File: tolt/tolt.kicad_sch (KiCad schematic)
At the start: 0 parts

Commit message: new file:   tolt/powerstage.kicad_sch 	modified:   tolt/stm32.kicad_sch 	modified:   tolt/tolt.kicad_pro 	modified:   tolt/tolt.kicad_sch
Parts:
- added J2: USB_C_Receptacle_USB2.0, Connector_USB:USB_C_Receptacle_G-Switch_GT-USB-7051x, symbol Connector:USB_C_Receptacle_USB2.0
- added R4, R5: 5k1, Resistor_SMD:R_0603_1608Metric, symbol Device:R
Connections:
- new net: J2.B5 (CC2), R5.2
- new net: J2.A5 (CC1), R4.2
- new net: J2.A4 (VBUS), J2.A9 (VBUS), J2.B4 (VBUS), J2.B9 (VBUS)
- new net: J2.A6 (D+), J2.B6 (D+)
- new net: J2.A7 (D-), J2.B7 (D-)
- new net GND: J2.A1 (GND), J2.A12 (GND), J2.B1 (GND), J2.B12 (GND), J2.S1 (SHIELD), R4.1, R5.1
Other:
- sheet mcu renamed logic
- added sheet powerstage (powerstage.kicad_sch)

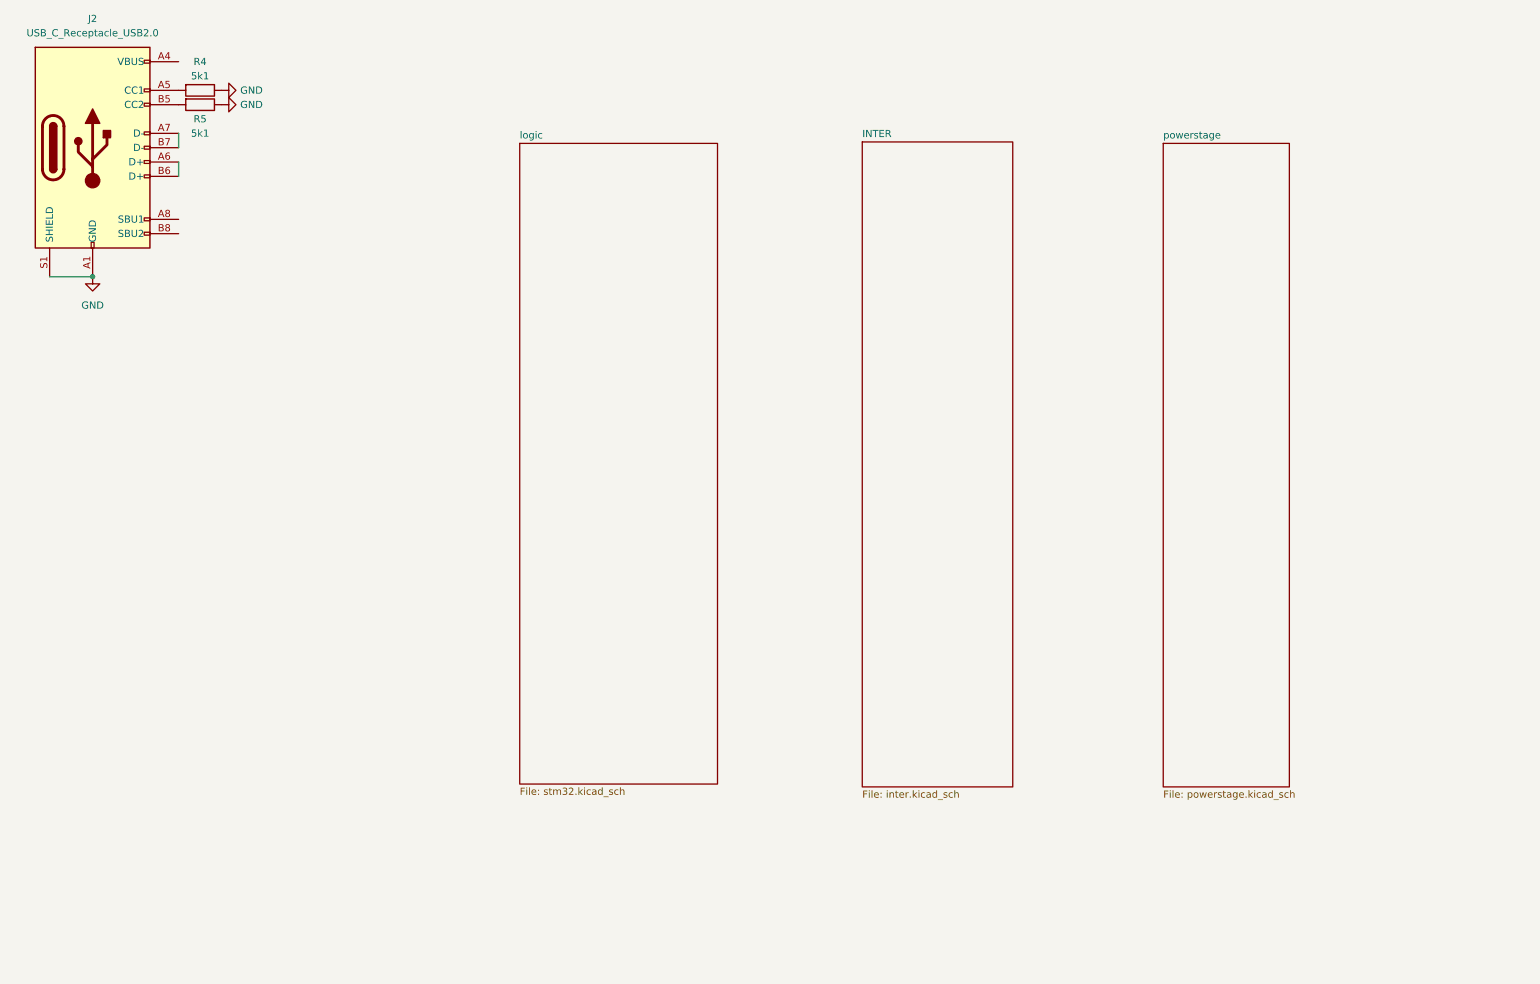
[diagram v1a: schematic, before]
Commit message: modified:   tolt/inter.kicad_sch 	modified:   tolt/stm32.kicad_sch 	modified:   tolt/tolt.kicad_sch
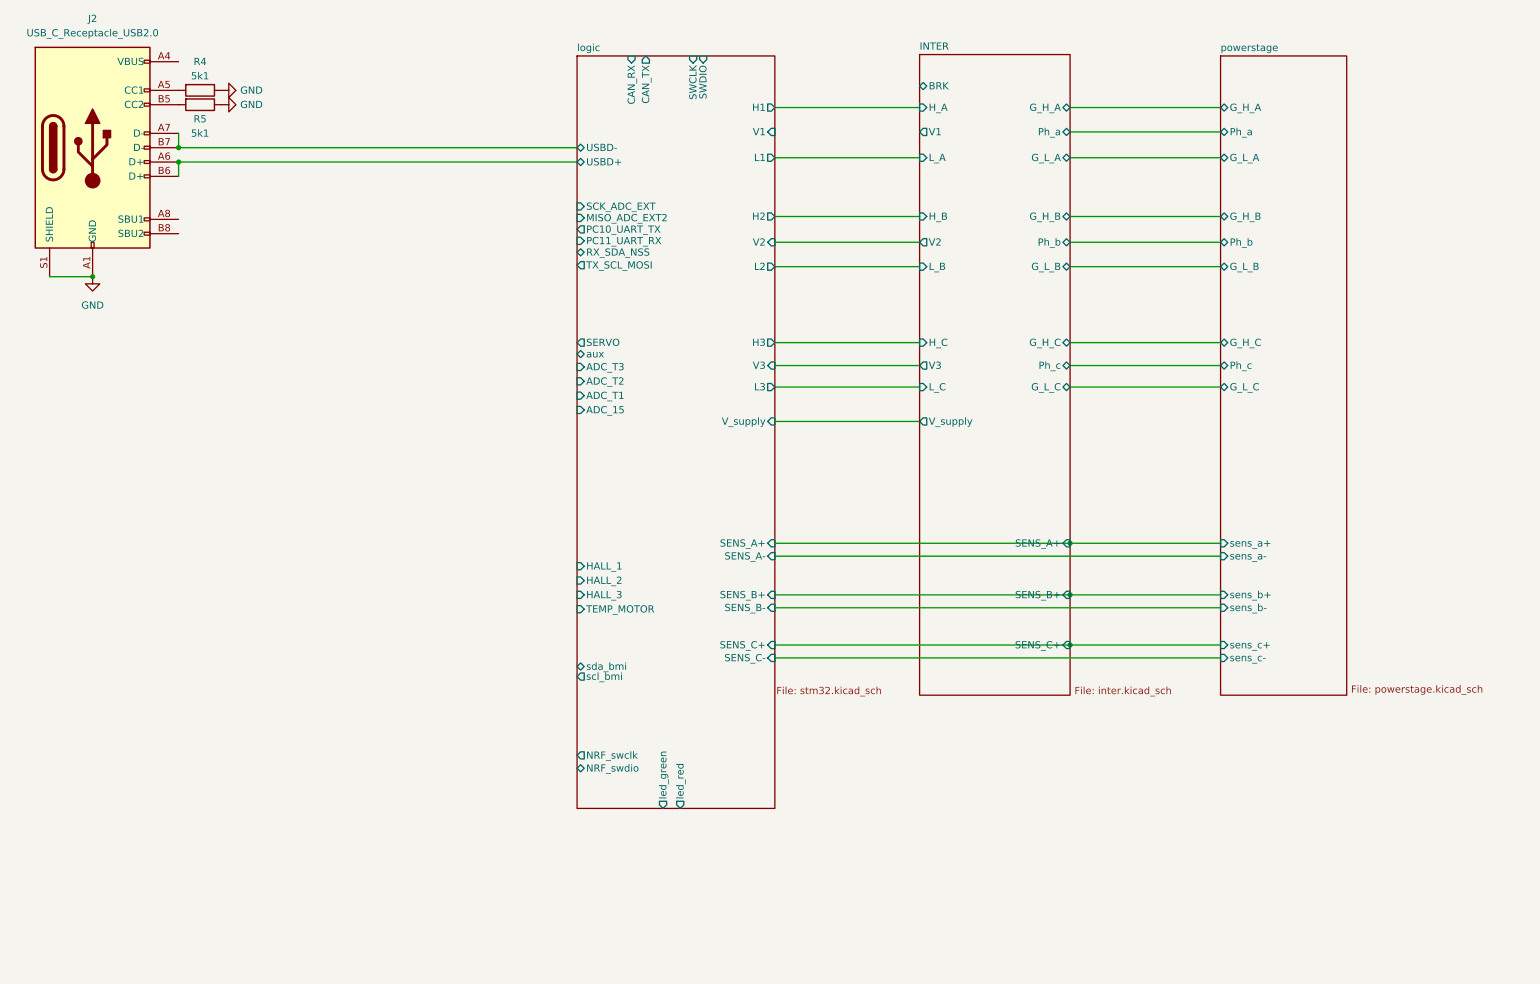
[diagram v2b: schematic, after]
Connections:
- net logic/USBD+: now reaches J2.A6 (D+), J2.B6 (D+)
- net logic/USBD-: now reaches J2.A7 (D-), J2.B7 (D-)
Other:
- sheet INTER ports: added BRK, G_H_A, G_H_B, G_H_C, G_L_A, G_L_B, G_L_C, H_A, H_B, H_C, L_A, L_B, L_C, Ph_a, Ph_b, Ph_c, SENS_A+, SENS_B+, SENS_C+, V1, V2, V3, V_supply; removed none
- sheet logic ports: added ADC_15, ADC_T1, ADC_T2, ADC_T3, CAN_RX, CAN_TX, H1, H2, H3, HALL_1, HALL_2, HALL_3, L1, L2, L3, MISO_ADC_EXT2, NRF_swclk, NRF_swdio, PC10_UART_TX, PC11_UART_RX, RX_SDA_NSS, SCK_ADC_EXT, SENS_A+, SENS_A-, SENS_B+, SENS_B-, SENS_C+, SENS_C-, SERVO, SWCLK, SWDIO, TEMP_MOTOR, TX_SCL_MOSI, USBD+, USBD-, V1, V2, V3, V_supply, aux, led_green, led_red, scl_bmi, sda_bmi; removed none
- sheet powerstage ports: added G_H_A, G_H_B, G_H_C, G_L_A, G_L_B, G_L_C, Ph_a, Ph_b, Ph_c, sens_a+, sens_a-, sens_b+, sens_b-, sens_c+, sens_c-; removed none

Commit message: modified:   tolt/inter.kicad_sch 	modified:   tolt/powerstage.kicad_sch 	modified:   tolt/stm32.kicad_sch 	modified:   tolt/tolt.kicad_sch
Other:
- sheet powerstage ports: added TEMP, TEMP1, TEMP2; removed none
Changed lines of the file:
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@@
+	(wire
+		(pts
+			(xy 149.352 98.298) (xy 228.346 98.298)
+		)
+		(stroke
+			(width 0)
+			(type default)
+		)
+	)
 	(wire
 		(pts
@@
 	(wire
 		(pts
+			(xy 149.352 93.726) (xy 228.346 93.726)
+		)
+		(stroke
+			(width 0)
+			(type default)
+		)
+	)
+	(wire
+		(pts
 			(xy 201.676 29.718) (xy 228.346 29.718)
 		)
@@
 		(pts
 			(xy 201.676 106.934) (xy 228.346 106.934)
+		)
+		(stroke
+			(width 0)
+			(type default)
+		)
+	)
+	(wire
+		(pts
+			(xy 149.352 96.012) (xy 228.346 96.012)
 		)
 		(stroke
@@
 		)
 		(pin "ADC_15" input
-			(at 114.3 83.312 180)
+			(at 114.3 97.028 180)
 			(effects
 				(font
@@
 		)
 		(pin "ADC_T1" input
-			(at 114.3 80.772 180)
-			(effects
-				(font
-					(size 1.27 1.27)
-				)
-				(justify left)
+			(at 149.352 98.298 0)
+			(effects
+				(font
+					(size 1.27 1.27)
+				)
+				(justify right)
 			)
 		)
 		(pin "ADC_T2" input
-			(at 114.3 78.232 180)
-			(effects
-				(font
-					(size 1.27 1.27)
-				)
-				(justify left)
+			(at 149.352 96.012 0)
+			(effects
+				(font
+					(size 1.27 1.27)
+				)
+				(justify right)
 			)
 		)
 		(pin "ADC_T3" input
-			(at 114.3 75.692 180)
-			(effects
-				(font
-					(size 1.27 1.27)
-				)
-				(justify left)
+			(at 149.352 93.726 0)
+			(effects
+				(font
+					(size 1.27 1.27)
+				)
+				(justify right)
 			)
 		)
 		(pin "aux" bidirectional
-			(at 114.3 73.406 180)
+			(at 114.3 94.996 180)
 			(effects
 				(font
@@
 		)
 		(pin "led_green" output
-			(at 129.54 153.924 270)
+			(at 140.462 153.924 270)
 			(effects
 				(font
@@
 		)
 		(pin "led_red" output
-			(at 132.588 153.924 270)
+			(at 143.51 153.924 270)
 			(effects
 				(font
@@
 		)
 		(pin "MISO_ADC_EXT2" input
-			(at 114.3 49.276 180)
+			(at 114.3 62.992 180)
 			(effects
 				(font
@@
 		)
 		(pin "NRF_swclk" output
-			(at 114.3 144.526 180)
+			(at 120.65 153.924 270)
 			(effects
 				(font
@@
 		)
 		(pin "NRF_swdio" bidirectional
-			(at 114.3 146.812 180)
+			(at 123.698 153.924 270)
 			(effects
 				(font
@@
 		)
 		(pin "PC10_UART_TX" output
-			(at 114.3 51.308 180)
+			(at 114.3 65.024 180)
 			(effects
 				(font
@@
 		)
 		(pin "PC11_UART_RX" input
-			(at 114.3 53.34 180)
+			(at 114.3 67.056 180)
 			(effects
 				(font
@@
 		)
 		(pin "RX_SDA_NSS" bidirectional
-			(at 114.3 55.372 180)
+			(at 114.3 69.088 180)
 			(effects
 				(font
@@
 		)
 		(pin "SCK_ADC_EXT" input
-			(at 114.3 47.244 180)
+			(at 114.3 60.96 180)
 			(effects
 				(font
@@
 		)
 		(pin "SERVO" output
-			(at 114.3 71.374 180)
+			(at 114.3 92.964 180)
 			(effects
 				(font
@@
 		)
 		(pin "TX_SCL_MOSI" output
-			(at 114.3 57.658 180)
+			(at 114.3 71.374 180)
 			(effects
 				(font
@@
 			(effects
 				(font
+					(size 1.27 1.27)
+				)
+				(justify left)
+			)
+		)
+		(pin "TEMP" output
+			(at 228.346 98.298 180)
+			(effects
+				(font
+					(size 1.27 1.27)
+				)
+				(justify left)
+			)
+		)
+		(pin "TEMP1" output
+			(at 228.346 96.012 180)
+			(effects
+				(font
+					(size 1.27 1.27)
+				)
+				(justify left)
+			)
+		)
+		(pin "TEMP2" output
+			(at 228.346 93.726 180)
+			(effects
+				(font

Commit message: Converters
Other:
- added sheet converters (converters.kicad_sch)
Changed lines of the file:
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@@
+	)
+	(sheet
+		(at 39.624 93.98)
+		(size 52.07 38.1)
+		(exclude_from_sim no)
+		(in_bom yes)
+		(on_board yes)
+		(dnp no)
+		(fields_autoplaced yes)
+		(stroke
+			(width 0.1524)
+			(type solid)
+		)
+		(fill
+			(color 0 0 0 0.0000)
+		)
+		(property "Sheetname" "converters"
+			(at 39.624 93.2684 0)
+			(effects
+				(font
+					(size 1.27 1.27)
+				)
+				(justify left bottom)
+			)
+		)
+		(property "Sheetfile" "converters.kicad_sch"
+			(at 39.624 132.6646 0)
+			(effects
+				(font
+					(size 1.27 1.27)
+				)
+				(justify left top)
+			)
+		)
+		(instances
+			(project "tolt"
+				(path "/38c63d96-01d7-4159-b7c0-aa8cee77c3e9"
+					(page "5")
+				)
+			)
+		)
 	)
 	(sheet

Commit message: .
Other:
- added sheet auxl (auxl.kicad_sch)
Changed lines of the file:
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@@
 			(project "tolt"
 				(path "/38c63d96-01d7-4159-b7c0-aa8cee77c3e9"
-					(page "2")
+					(page "3")
+				)
+			)
+		)
+	)
+	(sheet
+		(at 58.42 165.1)
+		(size 13.97 8.89)
+		(exclude_from_sim no)
+		(in_bom yes)
+		(on_board yes)
+		(dnp no)
+		(fields_autoplaced yes)
+		(stroke
+			(width 0.1524)
+			(type solid)
+		)
+		(fill
+			(color 0 0 0 0.0000)
+		)
+		(property "Sheetname" "auxl"
+			(at 58.42 164.3884 0)
+			(effects
+				(font
+					(size 1.27 1.27)
+				)
+				(justify left bottom)
+			)
+		)
+		(property "Sheetfile" "auxl.kicad_sch"
+			(at 58.42 174.5746 0)
+			(effects
+				(font
+					(size 1.27 1.27)
+				)
+				(justify left top)
+			)
+		)
+		(instances
+			(project "tolt"
+				(path "/38c63d96-01d7-4159-b7c0-aa8cee77c3e9"
+					(page "6")
 				)
 			)
@@
 			(project "tolt"
 				(path "/38c63d96-01d7-4159-b7c0-aa8cee77c3e9"
-					(page "5")
+					(page "2")
 				)
 			)
@@
 			(project "tolt"
 				(path "/38c63d96-01d7-4159-b7c0-aa8cee77c3e9"
-					(page "3")
+					(page "4")
 				)
 			)
@@
 			(project "tolt"
 				(path "/38c63d96-01d7-4159-b7c0-aa8cee77c3e9"
-					(page "4")
-				)
-			)
+					(page "5")
+				)
+			)

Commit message: Reapply "Merge branch 'main' of https://github.com/LJBoxx/bigtolt"
This reverts commit 10d1035653869a11abcc4dc45a35a471baa73785.
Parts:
- removed J2: USB_C_Receptacle_USB2.0, Connector_USB:USB_C_Receptacle_G-Switch_GT-USB-7051x, symbol Connector:USB_C_Receptacle_USB2.0
- removed R4, R5: 5k1, Resistor_SMD:R_0603_1608Metric, symbol Device:R
- added D22: green, symbol Device:LED
- added D26: red, symbol Device:LED
- added D27: blue, symbol Device:LED
- added R65, R66: 220r, Resistor_SMD:R_0603_1608Metric, symbol Device:R
- added R67: 1k, Resistor_SMD:R_0603_1608Metric, symbol Device:R
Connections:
- net GND: now also R65.1, R66.1, R67.1
- net logic/led_green: now also D22.2 (A)
- net logic/led_red: now also D26.2 (A)
- new net: D27.1 (K), R67.2
- new net: D26.1 (K), R66.2
- new net: D22.1 (K), R65.2
- new net VCC: D27.2 (A)
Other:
- added sheet IO (conn.kicad_sch)
- added sheet aux logic (auxl.kicad_sch)
- sheet logic ports: added rst; removed none

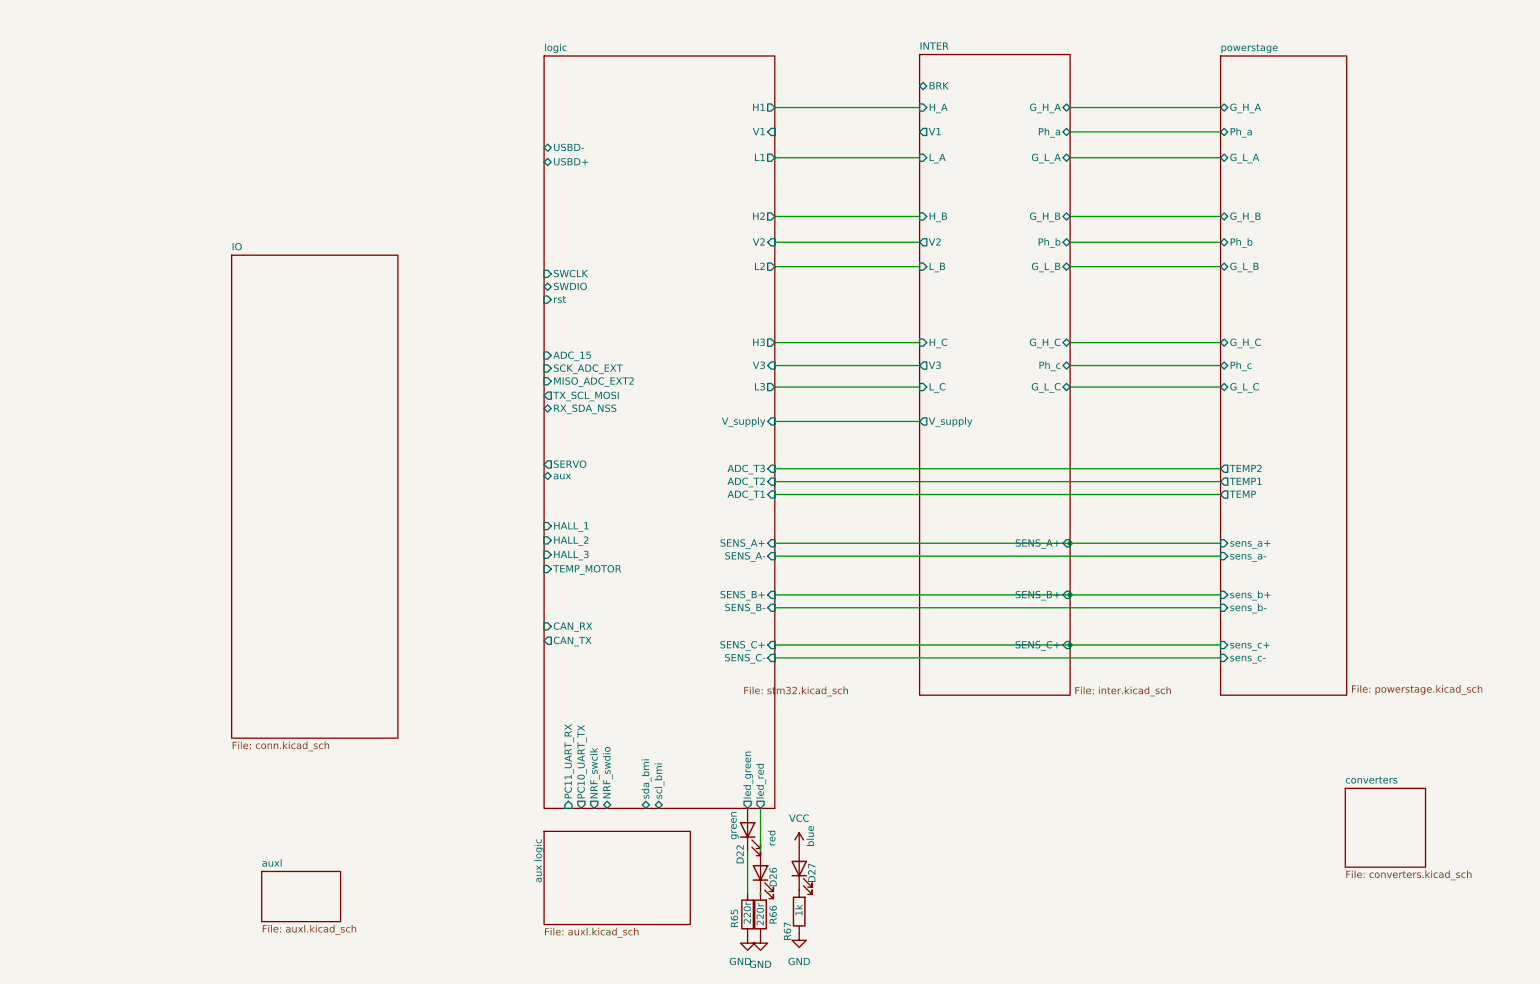
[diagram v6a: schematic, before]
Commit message: Revert "Merge branch 'main' of https://github.com/LJBoxx/bigtolt"
This reverts commit 648dc93627ac55c8b54fa74faadbb35a312ea564, reversing
changes made to 972c1c2491e13322900779e00755fdd65e6f8c8a.
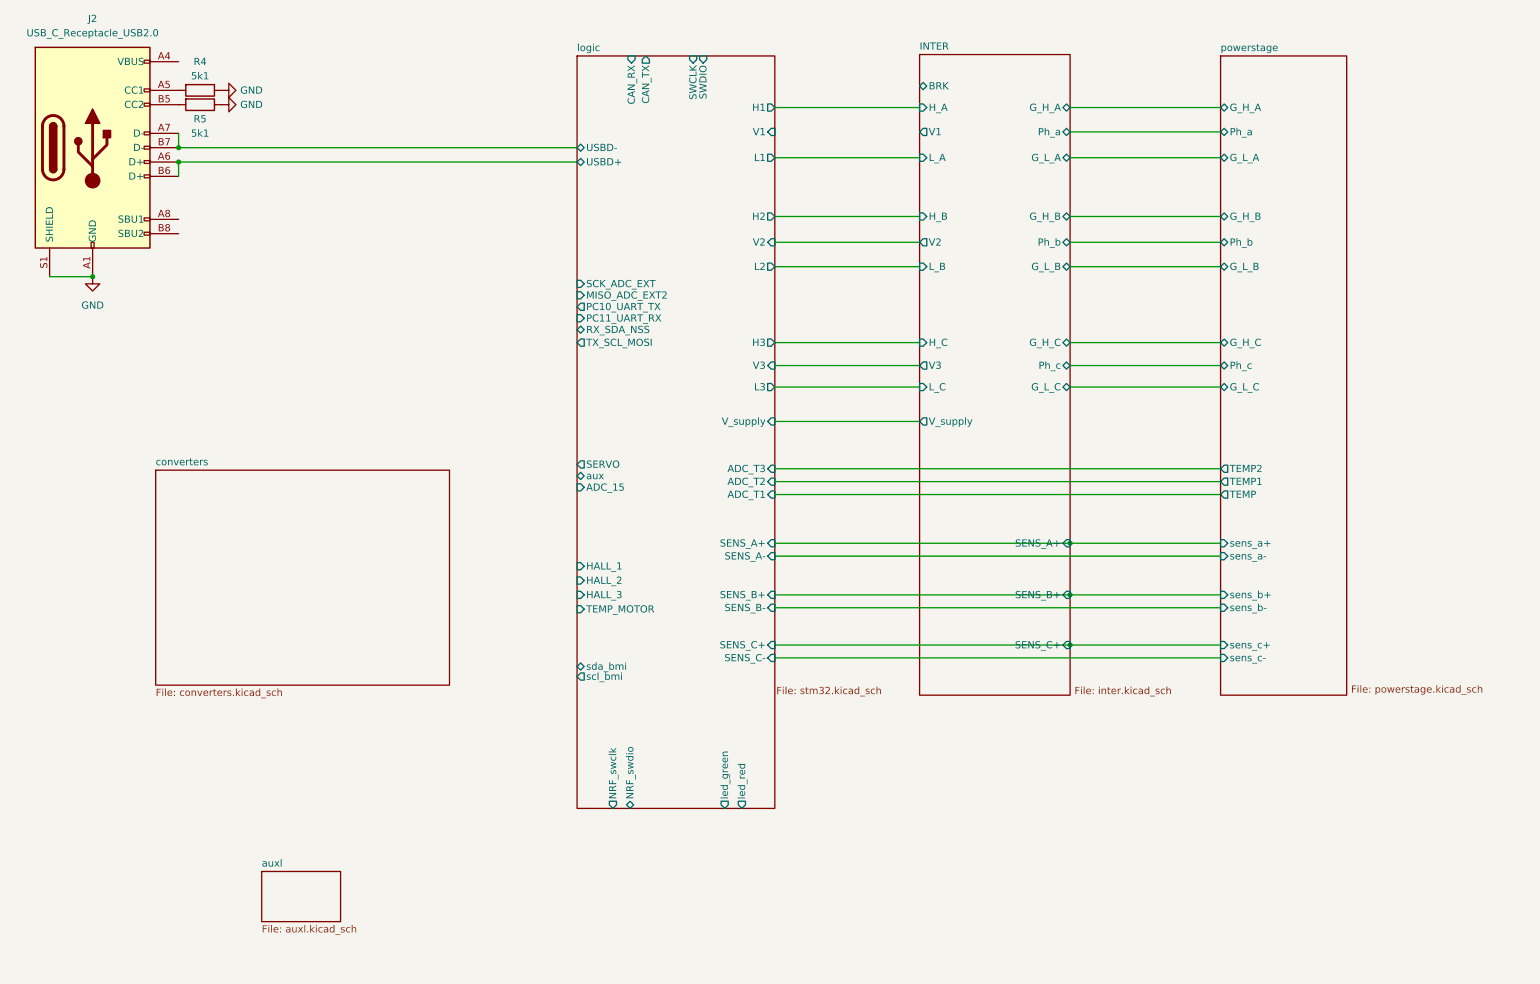
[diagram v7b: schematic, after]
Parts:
- removed D22: green, symbol Device:LED
- removed D26: red, symbol Device:LED
- removed D27: blue, symbol Device:LED
- removed R65, R66: 220r, Resistor_SMD:R_0603_1608Metric, symbol Device:R
- removed R67: 1k, Resistor_SMD:R_0603_1608Metric, symbol Device:R
- added J2: USB_C_Receptacle_USB2.0, Connector_USB:USB_C_Receptacle_G-Switch_GT-USB-7051x, symbol Connector:USB_C_Receptacle_USB2.0
- added R4, R5: 5k1, Resistor_SMD:R_0603_1608Metric, symbol Device:R
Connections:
- net GND: now also J2.A1 (GND), J2.A12 (GND), J2.B1 (GND), J2.B12 (GND), J2.S1 (SHIELD), R4.1, R5.1
- net logic/USBD+: now also J2.A6 (D+), J2.B6 (D+)
- net logic/USBD-: now also J2.A7 (D-), J2.B7 (D-)
- new net: J2.B5 (CC2), R5.2
- new net: J2.A5 (CC1), R4.2
- new net: J2.A4 (VBUS), J2.A9 (VBUS), J2.B4 (VBUS), J2.B9 (VBUS)
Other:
- removed sheet IO
- removed sheet aux logic
- sheet logic ports: added none; removed rst
